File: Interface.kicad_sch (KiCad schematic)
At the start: 0 parts

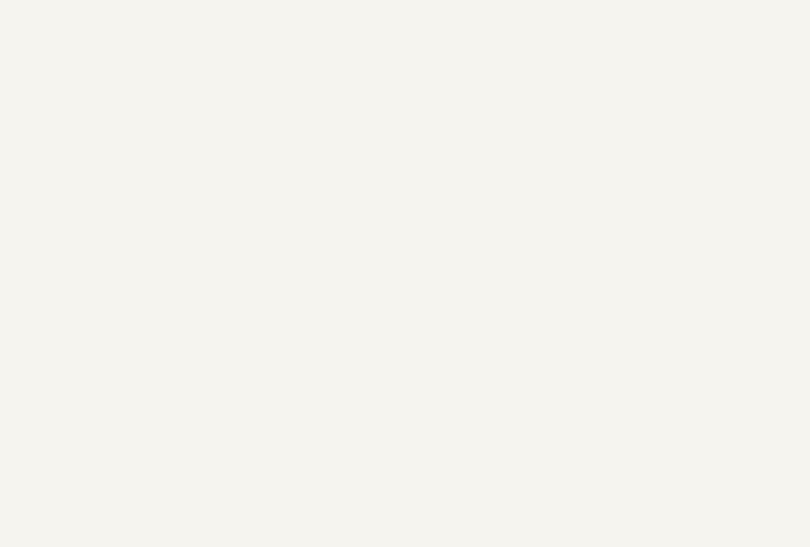
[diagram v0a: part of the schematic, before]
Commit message: connected the ICs to 5V digital power
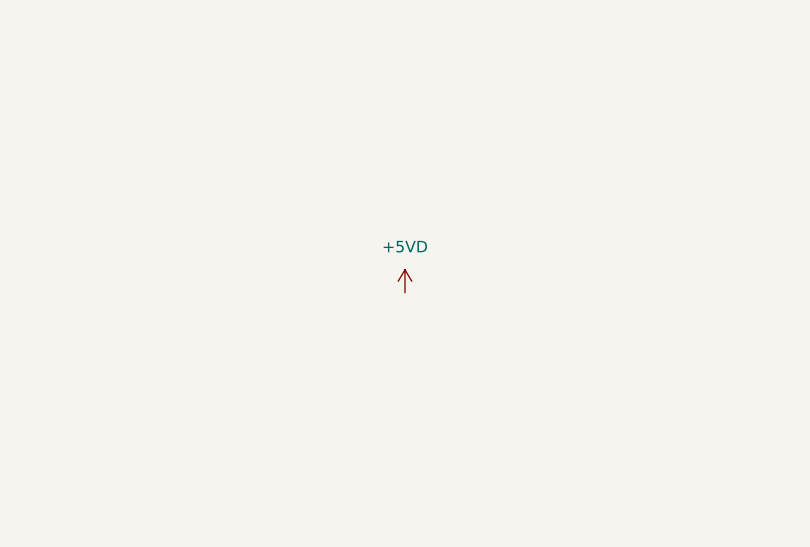
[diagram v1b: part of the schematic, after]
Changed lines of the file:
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@@
     (effects (font (size 1.27 1.27)) (justify right))
   )
+  (symbol (lib_id "power:+5VD") (at 134.62 67.31 0) (unit 1)
+    (in_bom yes) (on_board yes) (fields_autoplaced)
+    (property "Reference" "#PWR?" (id 0) (at 134.62 71.12 0)
+      (effects (font (size 1.27 1.27)) hide)
+    )
+    (property "Value" "+5VD" (id 1) (at 134.62 62.23 0))
+    (property "Footprint" "" (id 2) (at 134.62 67.31 0)
+      (effects (font (size 1.27 1.27)) hide)
+    )
+    (property "Datasheet" "" (id 3) (at 134.62 67.31 0)
+      (effects (font (size 1.27 1.27)) hide)
+    )
+    (pin "1")
+  )
 )
